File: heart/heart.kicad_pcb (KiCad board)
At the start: 2 copper layers, 0 parts

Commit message: [New] Complete heart board
Signed-off-by: Homalozoa X <nx.tardis@gmail.com>
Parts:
- added C1: 30pf 10V, Capacitor_SMD:C_0805_2012Metric, B.Cu at (185.4, 80.2)
- added C10: 470nF, 10%, 50V, Capacitor_SMD:C_0603_1608Metric, B.Cu at (130.4, 89.6)
- added C11: 10nf 50V, Capacitor_SMD:C_0402_1005Metric, B.Cu at (121.8, 82.1)
- added C12: 100uf 50V, Capacitor_SMD:C_0805_2012Metric, B.Cu at (127.7, 79.8)
- added C13: 100pF, 10%, 10V, Capacitor_SMD:C_0402_1005Metric, B.Cu at (137.8, 95.1)
- added C14: 100pF, 10%, 10V, Capacitor_SMD:C_0402_1005Metric, B.Cu at (135.4, 95.1)
- added C15: 1.5nf 50V, Capacitor_SMD:C_0402_1005Metric, B.Cu at (128.7, 82.9)
- added C16: 100nF, 10%, 50V, Capacitor_SMD:C_0402_1005Metric, B.Cu at (133.6, 93.1)
- added C17: 10uF, 10%, 50V, Capacitor_SMD:C_0603_1608Metric, B.Cu at (132.3, 93.4)
- added C18: 10uF, 10%, 50V, Capacitor_SMD:C_0603_1608Metric, B.Cu at (130.4, 91.1)
- added C19: 100nf 50V, Capacitor_SMD:C_0402_1005Metric, B.Cu at (125.9, 87.9)
- added C2: 30pf 10V, Capacitor_SMD:C_0805_2012Metric, B.Cu at (185.3, 73.8)
- added C20: 150pf 50V, Capacitor_SMD:C_0402_1005Metric, B.Cu at (123.1, 89.9)
- added C21: 1uf 10V, Capacitor_SMD:C_0402_1005Metric, B.Cu at (179.7, 79.7)
- added C22: 470pf 10V, Capacitor_SMD:C_0402_1005Metric, B.Cu at (179.7, 78.7)
- added C23: 1uf 10V, Capacitor_SMD:C_0402_1005Metric, B.Cu at (181.9, 78.4)
- added C24: 470pf 10V, Capacitor_SMD:C_0402_1005Metric, B.Cu at (182.9, 78.4)
- added C25: 22nf 10V, Capacitor_SMD:C_0805_2012Metric, B.Cu at (153.2, 87.7)
- added C26: 22nf 10V, Capacitor_SMD:C_0805_2012Metric, B.Cu at (153.2, 94.0)
- added C27: 1nf 2kv, Capacitor_SMD:C_1206_3216Metric, B.Cu at (156.5, 87.9)
- added C28: 4.7nf 2kv, Capacitor_SMD:C_1206_3216Metric, F.Cu at (154.0, 101.5)
- added C29: 4.7nf 2kv, Capacitor_SMD:C_1206_3216Metric, F.Cu at (154.0, 99.0)
- added C3: 1uf 10V, Capacitor_SMD:C_0402_1005Metric, B.Cu at (188.5, 103.2)
- added C4: 1uf 10V, Capacitor_SMD:C_0402_1005Metric, B.Cu at (190.4, 102.2)
- added C5: 100uf 6.3V, Capacitor_SMD:C_0805_2012Metric, B.Cu at (191.2, 103.8)
- added C6: 10pF, 10%, 50V, Capacitor_SMD:C_0402_1005Metric, B.Cu at (139.2, 87.4)
- added C7: 4.7uF 50V, Capacitor_SMD:C_0805_2012Metric, F.Cu at (122.8, 92.2)
- added C8: 10pF, 10%, 50V, Capacitor_SMD:C_0402_1005Metric, B.Cu at (134.1, 87.3)
- added C9: 10nF, 10%, 50V, Capacitor_SMD:C_0402_1005Metric, B.Cu at (133.3, 96.5)
- added D1: 30V, Diode_SMD:D_SMA, F.Cu at (119.7, 92.0)
- added D2: B340, Diode_SMD:D_SMC, B.Cu at (121.7, 76.4)
- added D3: 12V, Diode_SMD:D_SOD-323, B.Cu at (136.7, 100.3)
- added D4: 12V, Diode_SMD:D_SOD-323, B.Cu at (133.4, 100.3)
- added D5: NCD0402O1, LED_SMD:LED_0402_1005Metric, F.Cu at (185.0, 69.1)
- added D6: NCD0402C1, LED_SMD:LED_0402_1005Metric, F.Cu at (184.0, 69.1)
- added FB1: 220R, Resistor_SMD:R_0603_1608Metric, B.Cu at (177.4, 71.2)
- added FB2: 220R, Resistor_SMD:R_0603_1608Metric, B.Cu at (131.9, 87.5)
- added J1: Head, Rolling_Custom:XT30PW(2+2), F.Cu at (182.3, 104.9)
- added J10: UART_FLASH_ESP, Connector_JST:JST_GH_BM05B-GHS-TBT_1x05-1MP_P1.25mm_Vertical, F.Cu at (193.1, 69.9)
- added J11: RC02015, Connector_RJ:RJ45_Molex_0855135013_Vertical, F.Cu at (177.9, 91.1)
- added J2: Front, Rolling_Custom:XT30PW(2+2), F.Cu at (167.8, 78.5)
- added J3: Leg_L, Rolling_Custom:XT30PW(2+2), F.Cu at (138.9, 78.5)
- added J4: Leg_R, Rolling_Custom:XT30PW(2+2), F.Cu at (138.9, 104.9)
- added J5: Arm_L, Rolling_Custom:XT30PW(2+2), F.Cu at (153.4, 78.5)
- added J6: Arm_R, Rolling_Custom:XT30PW(2+2), F.Cu at (153.4, 104.9)
- added J7: Light, Rolling_Custom:XT30PW(2+2), F.Cu at (167.8, 104.9)
- added J8: Power_IN, Rolling_Custom:AMASS_XT60PW-F, F.Cu at (114.0, 85.5)
- added J9: Power_Back, Rolling_Custom:AMASS_XT60PW-M, F.Cu at (109.0, 101.7)
- added L1: 15uh, Inductor_SMD:L_0603_1608Metric, B.Cu at (122.4, 80.8)
- added Q1: Q_NPN_BCE, Package_TO_SOT_SMD:SOT-23, F.Cu at (191.9, 77.3)
- added Q2: Q_NPN_BCE, Package_TO_SOT_SMD:SOT-23, F.Cu at (196.1, 78.5)
- added Q4: FH1404G6, Rolling_Custom:PDFN5X6-8L, F.Cu at (125.9, 100.2)
- added Q5: FH1404G6, Rolling_Custom:PDFN5X6-8L, F.Cu at (125.8, 106.1)
- added Q6: FH1404G6, Rolling_Custom:PDFN5X6-8L, B.Cu at (126.0, 106.1)
- added R1: 10k, Resistor_SMD:R_0402_1005Metric, F.Cu at (192.1, 80.0)
- added R15: 499r, Resistor_SMD:R_0402_1005Metric, F.Cu at (195.0, 74.9)
- added R16: 33k, Resistor_SMD:R_0402_1005Metric, B.Cu at (133.3, 95.5)
- added R17: 3k, Resistor_SMD:R_0402_1005Metric, B.Cu at (131.4, 95.5)
- added R18: 120R, Resistor_SMD:R_0402_1005Metric, B.Cu at (136.1, 97.6)
- added R19: 10k, Resistor_SMD:R_0402_1005Metric, B.Cu at (127.7, 82.9)
- added R2: 10k, Resistor_SMD:R_0402_1005Metric, F.Cu at (192.7, 74.5)
- added R20: 5.9k, Resistor_SMD:R_0402_1005Metric, B.Cu at (123.1, 88.9)
- added R21: 549R, Resistor_SMD:R_0201_0603Metric, B.Cu at (125.9, 89.6)
- added R22: 10k, Resistor_SMD:R_0402_1005Metric, B.Cu at (185.0, 71.1)
- added R23: 10k, Resistor_SMD:R_0402_1005Metric, B.Cu at (184.0, 71.1)
- added R24: 12.1k, Resistor_SMD:R_0201_0603Metric, B.Cu at (181.9, 71.3)
- added R25: 49.9r, Resistor_SMD:R_0402_1005Metric, F.Cu at (147.6, 95.9)
- added R26: 49.9r, Resistor_SMD:R_0402_1005Metric, F.Cu at (147.7, 92.7)
- added R27: 49.9r, Resistor_SMD:R_0402_1005Metric, F.Cu at (147.7, 88.9)
- added R28: 49.9r, Resistor_SMD:R_0402_1005Metric, F.Cu at (147.7, 86.4)
- added R29: 75r, Resistor_SMD:R_0402_1005Metric, B.Cu at (158.9, 94.1)
- added R3: 33r, Resistor_SMD:R_0402_1005Metric, B.Cu at (175.5, 77.7)
- added R30: 75r, Resistor_SMD:R_0402_1005Metric, B.Cu at (158.9, 87.7)
- added R31: 332r, Resistor_SMD:R_0402_1005Metric, F.Cu at (185.0, 71.1)
- added R32: 332r, Resistor_SMD:R_0402_1005Metric, F.Cu at (184.0, 71.1)
- added R34: 75r, Resistor_SMD:R_0402_1005Metric, B.Cu at (160.0, 96.3)
- added R35: 75r, Resistor_SMD:R_0402_1005Metric, B.Cu at (160.0, 95.2)
- added R4: 10k, Resistor_SMD:R_0402_1005Metric, B.Cu at (188.5, 102.2)
- added R5: 470r, Resistor_SMD:R_0402_1005Metric, B.Cu at (175.5, 79.6)
- added T1: H1102NLT, Rolling_Custom:XFMR_H1102NLT, F.Cu at (154.5, 90.8)
- added U1: ESP32-WROVER-E, Espressif:ESP32-WROVER-E, B.Cu at (182.3, 91.3)
- added U2: TPS5430DDAR, Rolling_Custom:TPS5430DDAR, B.Cu at (121.6, 85.5)
- added U3: TCAN4550RGYRQ1, Rolling_Custom:VQFN20, B.Cu at (136.6, 91.9)
- added U4: LAN8720A, Package_DFN_QFN:QFN-24-1EP_4x4mm_P0.5mm_EP2.6x2.6mm, B.Cu at (180.3, 74.7)
- added Y1: 25MHz, Crystal:Crystal_SMD_3225-4Pin_3.2x2.5mm, B.Cu at (185.3, 77.0)
- added Y2: 40M, Oscillator:Oscillator_SMD_EuroQuartz_XO32-4Pin_3.2x2.5mm, B.Cu at (136.7, 87.1)
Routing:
- net GND: track 0.00 -> 467.4 mm, vias 0 -> 7
- net PWR_EXPORT: track 0.00 -> 193.8 mm
- net +3V3: track 0.00 -> 124.1 mm, vias 0 -> 6
- net CAN_L: track 0.00 -> 122.2 mm, vias 0 -> 1
- net CAN_H: track 0.00 -> 120.4 mm, vias 0 -> 1
- net PWRCT_3: track 0.00 -> 65.4 mm, vias 0 -> 2
- net VDDA: track 0.00 -> 60.5 mm, vias 0 -> 2
- net PWRCT_1: track 0.00 -> 58.7 mm, vias 0 -> 2
- net PWRCT_2: track 0.00 -> 57.8 mm, vias 0 -> 2
- net TCAN_INT: track 0.00 -> 54.6 mm, vias 0 -> 2
- net TCAN_WKRQ: track 0.00 -> 53.3 mm, vias 0 -> 2
- net ETH_RXP: track 0.00 -> 51.7 mm, vias 0 -> 2
- net +24V: track 0.00 -> 48.4 mm, vias 0 -> 2
- net ETH_RXN: track 0.00 -> 48.4 mm, vias 0 -> 2
- net TCAN_RST: track 0.00 -> 46.6 mm, vias 0 -> 2
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- added copper zone on In2.Cu, net +24V
- added copper zone on B.Cu, net +3V3
- added copper zone on F.Cu, net GND
- added copper zone on In1.Cu, net GND
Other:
- board outline added: 110 x 51 mm
- copper layers 2 -> 4

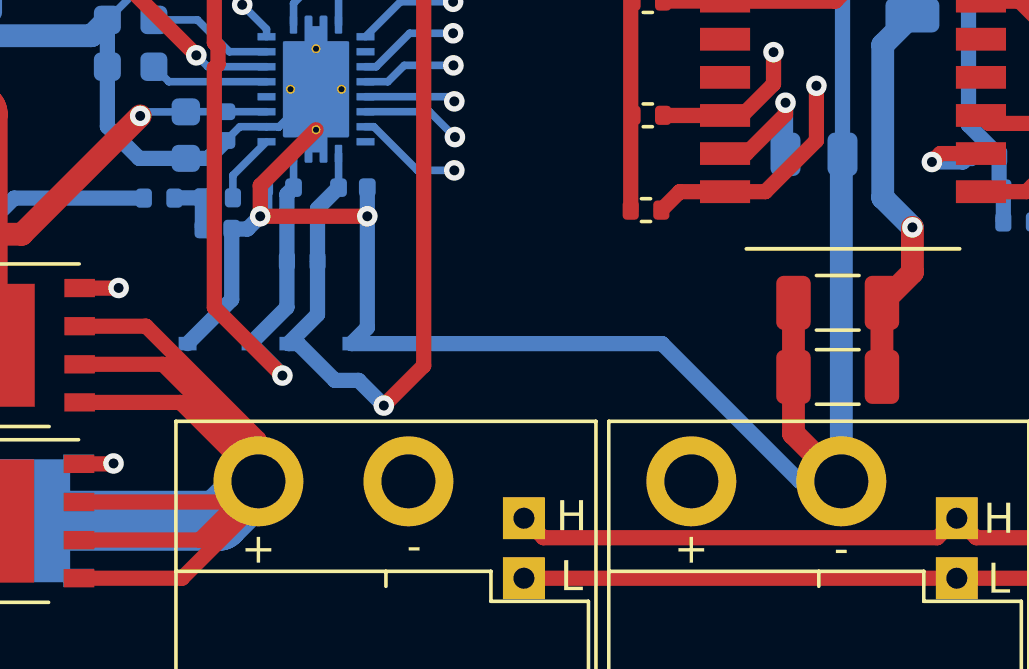
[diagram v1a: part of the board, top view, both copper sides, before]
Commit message: [Modify] Tune length of CAN bus wires
Signed-off-by: Homalozoa X <nx.tardis@gmail.com>
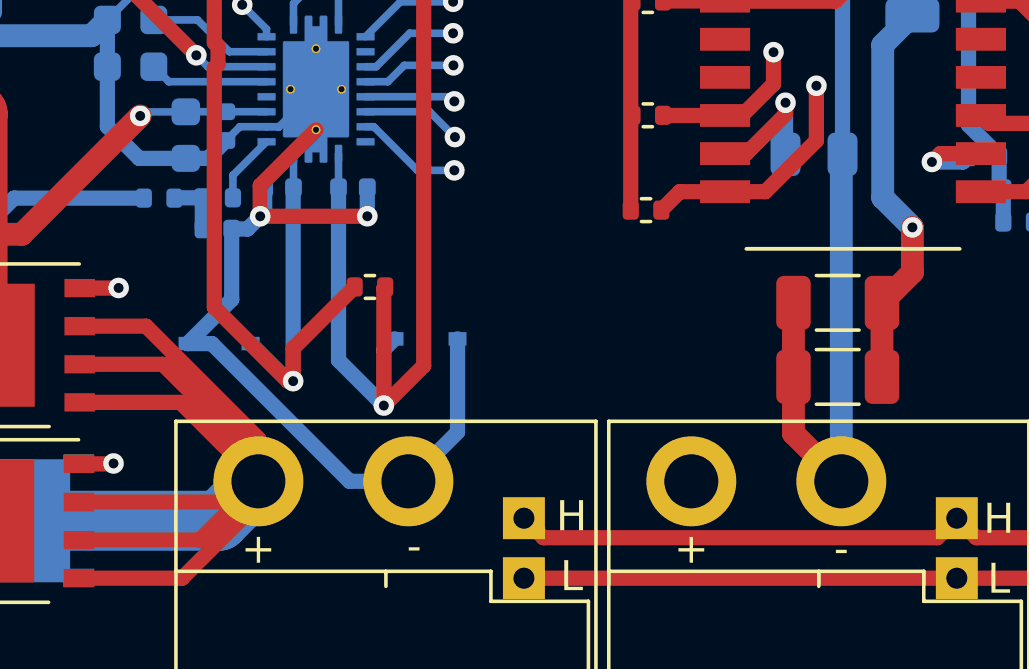
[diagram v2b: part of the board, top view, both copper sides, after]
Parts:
- R18: moved to F.Cu
- moved D3 3.54 mm to (140.3, 100.2)
- moved R18 2.41 mm to (138.4, 98.5)
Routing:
- net GND: track 467.4 -> 488.1 mm
- net CAN_H: track 120.4 -> 125.5 mm
- net CAN_L: track 122.2 -> 126.5 mm
